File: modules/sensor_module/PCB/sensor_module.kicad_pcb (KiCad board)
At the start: 2 copper layers, 76 x 76 mm, 66 parts, among them J1 Screw_Terminal_01x02, J2 Conn_01x06_Socket, J3 Conn_01x03_Socket, SW1 SW_SPDT, U1 AMS1117-3.3, U2 AMS1117-5, U3 ESP-12E, U4 LM393, U5 MQ-5, U6 LM393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

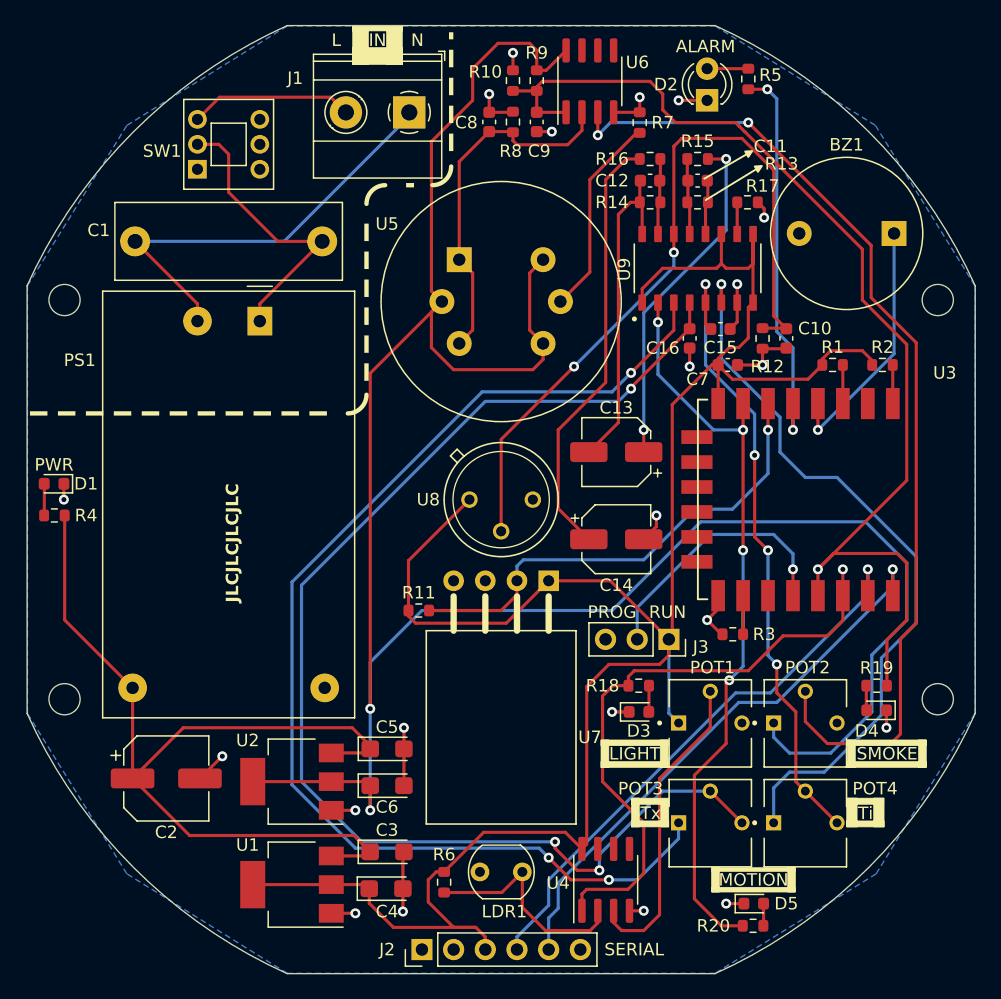
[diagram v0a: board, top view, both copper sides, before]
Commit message: ON-OFF module hardware updated to V2
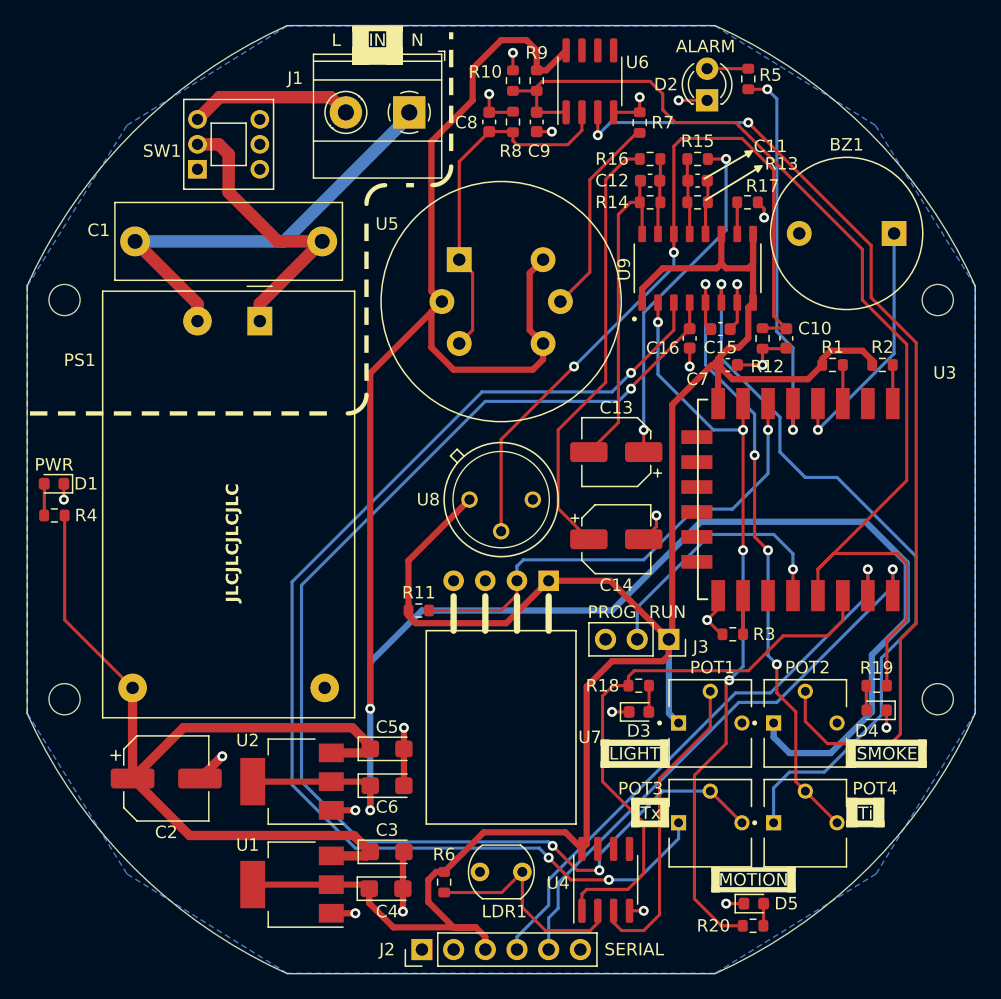
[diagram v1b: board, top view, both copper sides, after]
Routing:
- net LIGHT: track 48.9 -> 47.5 mm, vias 1 -> 0
- net +3.3V: track 179.4 -> 178.3 mm
- net SMOKE: vias 1 -> 0
